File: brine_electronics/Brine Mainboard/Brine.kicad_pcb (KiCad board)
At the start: 2 copper layers, 30.5 x 42.7 mm, 15 parts, among them J1 Conn_01x02_Socket, J2 VL53L1X, U1 XIAO-ESP32-S3-SMD

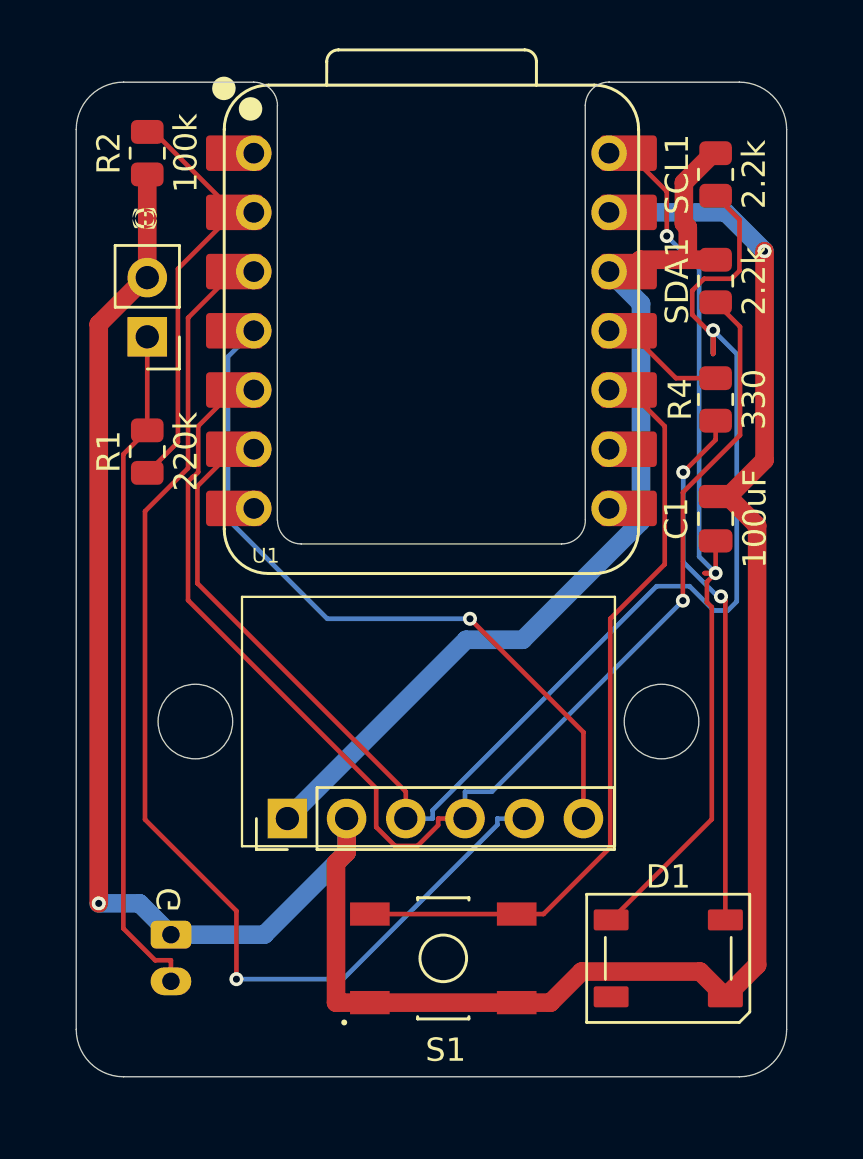
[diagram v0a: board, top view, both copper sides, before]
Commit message: Created integrated distance sensor
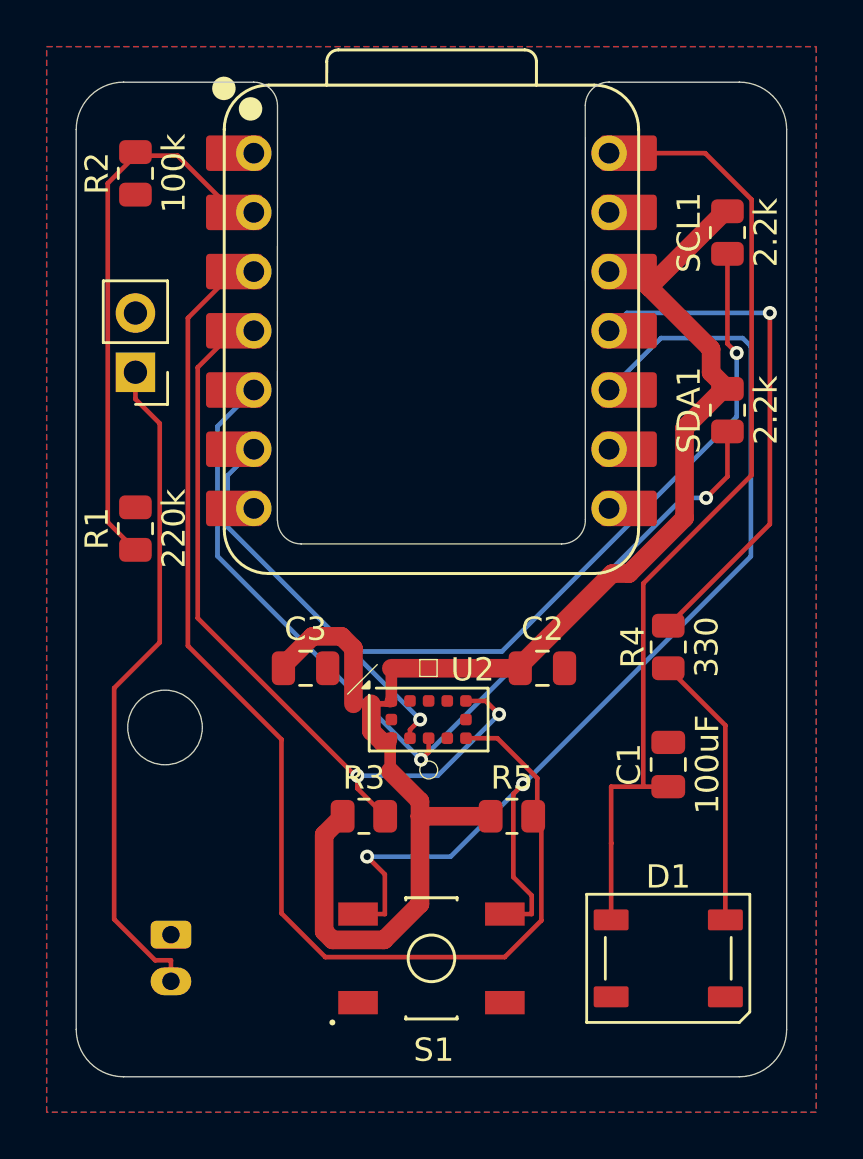
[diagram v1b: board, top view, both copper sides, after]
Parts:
- removed H1, H2: MountingHole, MountingHole:MountingHole_3.2mm_M3
- removed J2: VL53L1X, Connector_PinHeader_2.54mm:PinHeader_1x06_P2.54mm_Vertical
- added C2: 4.7uF, Capacitor_SMD:C_0805_2012Metric, F.Cu at (157.2, 95.2)
- added C3: 0.1uF, Capacitor_SMD:C_0805_2012Metric, F.Cu at (147.0, 95.2)
- added H3: Antenna, MountingHole:MountingHole_3.2mm_M3, F.Cu at (141.0, 97.8)
- added R3: 10k, Resistor_SMD:R_0805_2012Metric, F.Cu at (149.5, 101.6)
- added R5: 10k, Resistor_SMD:R_0805_2012Metric, F.Cu at (155.9, 101.6)
- added U2: VL53L1CXV0FY1, Sensor_Distance:ST_VL53L1x, F.Cu at (152.3, 97.5)
- moved R4 10.8 mm to (162.6, 94.3)
- moved C1 10.7 mm to (162.6, 99.4)
- moved SDA1 5.56 mm to (165.1, 84.2)
- moved R1 3.34 mm to (139.7, 89.3)
- moved SCL1 2.54 mm to (165.1, 76.6)
- moved BATT1 1.60 mm to (139.7, 82.5)
- moved R2 1.00 mm to (139.7, 74.0)
- moved S1 0.51 mm to (152.4, 107.7)
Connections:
- net BUTTON renamed /Button/BUTTON
- net LED renamed /RGB LED/LED
- net LIFE renamed /Battery Monitor/LIFE
- net SCL renamed /Distance Sensor/SCL
- net SDA renamed /Distance Sensor/SDA
- BATT1 pad 1: BATT -> /Battery/BATT
- J1 pad 2: BATT -> /Battery/BATT
- R1 pad 2: BATT -> /Battery Monitor/BATT
- U1 pad 3: GPIO1 -> /Distance Sensor/GPIO1
- U1 pad 4: XSHUT -> /Distance Sensor/XSHUT
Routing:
- net GND: track 114.5 -> 0.00 mm, vias 2 -> 0
- net /Distance Sensor/GPIO1: track 0.00 -> 53.5 mm
- net GPIO1: track 49.8 -> 0.00 mm, vias 1 -> 0
- net /Distance Sensor/XSHUT: track 0.00 -> 34.5 mm, vias 0 -> 2
- net XSHUT: track 32.1 -> 0.00 mm, vias 1 -> 0
- net BATT: track 29.3 -> 0.00 mm
- net /Battery/BATT: track 0.00 -> 28.8 mm
- net +3.3V: track 41.8 -> 66.7 mm
- net /Distance Sensor/SCL: track 64.5 -> 45.1 mm, vias 1 -> 2
- net /RGB LED/LED: track 5.41 -> 23.3 mm, vias 0 -> 1
- net /Button/BUTTON: track 33.6 -> 50.0 mm, vias 0 -> 2
- net /Distance Sensor/SDA: track 56.7 -> 42.1 mm, vias 1 -> 2
- net Net-(D1-DIN): track 24.1 -> 11.8 mm, vias 2 -> 0
- net /Battery Monitor/LIFE: track 18.7 -> 24.1 mm
- net +5V: track 39.6 -> 42.2 mm, vias 2 -> 0
- added copper zone on B.Cu, net GND
- added copper zone on F.Cu, net GND
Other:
- board text added: "04/03/26"
- board text added: "Brine Monitor"
- board text added: "Version 06"
- board text removed: "11/28/25"
- board text removed: "Dev Board"
- board text removed: "G"
- board text removed: "Version 05"
